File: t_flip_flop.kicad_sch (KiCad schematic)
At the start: 3 parts, among them U4 4011

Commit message: routing done
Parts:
- renumbered C2 to C13, R11 to R6, U4 to U5
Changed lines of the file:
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@@
   (symbol (lib_id "4xxx:4011") (at 92.71 39.37 0) (unit 1)
     (in_bom yes) (on_board yes) (fields_autoplaced)
-    (property "Reference" "U4" (id 0) (at 92.71 31.8602 0))
+    (property "Reference" "U5" (id 0) (at 92.71 31.8602 0))
     (property "Value" "4011" (id 1) (at 92.71 34.3971 0))
     (property "Footprint" "Package_SO:SOIC-14_3.9x8.7mm_P1.27mm" (id 2) (at 92.71 39.37 0)
@@
   (symbol (lib_id "power:VDD") (at 29.21 36.83 0) (unit 1)
     (in_bom yes) (on_board yes)
-    (property "Reference" "#PWR011" (id 0) (at 29.21 40.64 0)
+    (property "Reference" "#PWR024" (id 0) (at 29.21 40.64 0)
       (effects (font (size 1.27 1.27)) hide)
     )
@@
   (symbol (lib_id "4xxx:4011") (at 92.71 59.69 0) (unit 2)
     (in_bom yes) (on_board yes) (fields_autoplaced)
-    (property "Reference" "U4" (id 0) (at 92.71 52.1802 0))
+    (property "Reference" "U5" (id 0) (at 92.71 52.1802 0))
     (property "Value" "4011" (id 1) (at 92.71 54.7171 0))
     (property "Footprint" "Package_SO:SOIC-14_3.9x8.7mm_P1.27mm" (id 2) (at 92.71 59.69 0)
@@
   (symbol (lib_id "4xxx:4011") (at 115.57 41.91 0) (unit 3)
     (in_bom yes) (on_board yes) (fields_autoplaced)
-    (property "Reference" "U4" (id 0) (at 115.57 34.4002 0))
+    (property "Reference" "U5" (id 0) (at 115.57 34.4002 0))
     (property "Value" "4011" (id 1) (at 115.57 36.9371 0))
     (property "Footprint" "Package_SO:SOIC-14_3.9x8.7mm_P1.27mm" (id 2) (at 115.57 41.91 0)
@@
   (symbol (lib_id "4xxx:4011") (at 115.57 57.15 0) (unit 4)
     (in_bom yes) (on_board yes) (fields_autoplaced)
-    (property "Reference" "U4" (id 0) (at 115.57 49.6402 0))
+    (property "Reference" "U5" (id 0) (at 115.57 49.6402 0))
     (property "Value" "4011" (id 1) (at 115.57 52.1771 0))
     (property "Footprint" "Package_SO:SOIC-14_3.9x8.7mm_P1.27mm" (id 2) (at 115.57 57.15 0)
@@
   (symbol (lib_id "Device:C") (at 57.785 53.34 0) (unit 1)
     (in_bom yes) (on_board yes) (fields_autoplaced)
-    (property "Reference" "C2" (id 0) (at 60.706 52.5053 0)
+    (property "Reference" "C13" (id 0) (at 60.706 52.5053 0)
       (effects (font (size 1.27 1.27)) (justify left))
     )
@@
   (symbol (lib_id "Device:R") (at 68.58 53.34 180) (unit 1)
     (in_bom yes) (on_board yes) (fields_autoplaced)
-    (property "Reference" "R11" (id 0) (at 70.358 52.5053 0)
+    (property "Reference" "R6" (id 0) (at 70.358 52.5053 0)
       (effects (font (size 1.27 1.27)) (justify right))
     )
@@
   (symbol (lib_id "power:VSS") (at 57.785 57.15 180) (unit 1)
     (in_bom yes) (on_board yes) (fields_autoplaced)
-    (property "Reference" "#PWR014" (id 0) (at 57.785 53.34 0)
+    (property "Reference" "#PWR026" (id 0) (at 57.785 53.34 0)
       (effects (font (size 1.27 1.27)) hide)
     )
@@
   (symbol (lib_id "power:VSS") (at 29.21 62.23 180) (unit 1)
     (in_bom yes) (on_board yes) (fields_autoplaced)
-    (property "Reference" "#PWR012" (id 0) (at 29.21 58.42 0)
+    (property "Reference" "#PWR025" (id 0) (at 29.21 58.42 0)
       (effects (font (size 1.27 1.27)) hide)
     )
@@
   (symbol (lib_id "4xxx:4011") (at 29.21 49.53 0) (unit 5)
     (in_bom yes) (on_board yes) (fields_autoplaced)
-    (property "Reference" "U4" (id 0) (at 35.052 48.6953 0)
+    (property "Reference" "U5" (id 0) (at 35.052 48.6953 0)
       (effects (font (size 1.27 1.27)) (justify left))
     )

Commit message: ready to order
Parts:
- U5: value 4011 -> 4093; symbol 4xxx:4011 -> 4xxx:HEF4093B; JLC C194334 -> C194332
- renumbered C13 to C17
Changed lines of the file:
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@@
     (effects (font (size 1.27 1.27)) (justify left))
   )
-  (symbol (lib_id "4xxx:4011") (at 92.71 39.37 0) (unit 1)
+  (symbol (lib_id "4xxx:HEF4093B") (at 92.71 39.37 0) (unit 1)
     (in_bom yes) (on_board yes) (fields_autoplaced)
     (property "Reference" "U5" (id 0) (at 92.71 31.8602 0))
-    (property "Value" "4011" (id 1) (at 92.71 34.3971 0))
+    (property "Value" "4093" (id 1) (at 92.71 34.3971 0))
     (property "Footprint" "Package_SO:SOIC-14_3.9x8.7mm_P1.27mm" (id 2) (at 92.71 39.37 0)
       (effects (font (size 1.27 1.27)) hide)
     )
-    (property "Datasheet" "https://datasheet.lcsc.com/lcsc/1811031937_HGSEMI-CD4011BM-TR_C194334.pdf" (id 3) (at 92.71 39.37 0)
-      (effects (font (size 1.27 1.27)) hide)
-    )
-    (property "JLC" "C194334" (id 4) (at 92.71 39.37 0)
+    (property "Datasheet" "https://datasheet.lcsc.com/lcsc/2107091824_HGSEMI-CD4093BM-TR_C194332.pdf" (id 3) (at 92.71 39.37 0)
+      (effects (font (size 1.27 1.27)) hide)
+    )
+    (property "JLC" "C194332" (id 4) (at 92.71 39.37 0)
       (effects (font (size 1.27 1.27)) hide)
     )
@@
   (symbol (lib_id "power:VDD") (at 29.21 36.83 0) (unit 1)
     (in_bom yes) (on_board yes)
-    (property "Reference" "#PWR024" (id 0) (at 29.21 40.64 0)
+    (property "Reference" "#PWR026" (id 0) (at 29.21 40.64 0)
       (effects (font (size 1.27 1.27)) hide)
     )
@@
     (pin "1")
   )
-  (symbol (lib_id "4xxx:4011") (at 92.71 59.69 0) (unit 2)
+  (symbol (lib_id "4xxx:HEF4093B") (at 92.71 59.69 0) (unit 2)
     (in_bom yes) (on_board yes) (fields_autoplaced)
     (property "Reference" "U5" (id 0) (at 92.71 52.1802 0))
-    (property "Value" "4011" (id 1) (at 92.71 54.7171 0))
+    (property "Value" "4093" (id 1) (at 92.71 54.7171 0))
     (property "Footprint" "Package_SO:SOIC-14_3.9x8.7mm_P1.27mm" (id 2) (at 92.71 59.69 0)
       (effects (font (size 1.27 1.27)) hide)
     )
-    (property "Datasheet" "https://datasheet.lcsc.com/lcsc/1811031937_HGSEMI-CD4011BM-TR_C194334.pdf" (id 3) (at 92.71 59.69 0)
-      (effects (font (size 1.27 1.27)) hide)
-    )
-    (property "JLC" "C194334" (id 4) (at 92.71 59.69 0)
-      (effects (font (size 1.27 1.27)) hide)
-    )
-    (pin "1")
-    (pin "2")
-    (pin "3")
-    (pin "4")
-    (pin "5")
-    (pin "6")
-    (pin "10")
-    (pin "8")
-    (pin "9")
-    (pin "11")
-    (pin "12")
-    (pin "13")
-    (pin "14")
-    (pin "7")
-  )
-  (symbol (lib_id "4xxx:4011") (at 115.57 41.91 0) (unit 3)
+    (property "Datasheet" "https://datasheet.lcsc.com/lcsc/2107091824_HGSEMI-CD4093BM-TR_C194332.pdf" (id 3) (at 92.71 59.69 0)
+      (effects (font (size 1.27 1.27)) hide)
+    )
+    (property "JLC" "C194332" (id 4) (at 92.71 59.69 0)
+      (effects (font (size 1.27 1.27)) hide)
+    )
+    (pin "1")
+    (pin "2")
+    (pin "3")
+    (pin "4")
+    (pin "5")
+    (pin "6")
+    (pin "10")
+    (pin "8")
+    (pin "9")
+    (pin "11")
+    (pin "12")
+    (pin "13")
+    (pin "14")
+    (pin "7")
+  )
+  (symbol (lib_id "4xxx:HEF4093B") (at 115.57 41.91 0) (unit 3)
     (in_bom yes) (on_board yes) (fields_autoplaced)
     (property "Reference" "U5" (id 0) (at 115.57 34.4002 0))
-    (property "Value" "4011" (id 1) (at 115.57 36.9371 0))
+    (property "Value" "4093" (id 1) (at 115.57 36.9371 0))
     (property "Footprint" "Package_SO:SOIC-14_3.9x8.7mm_P1.27mm" (id 2) (at 115.57 41.91 0)
       (effects (font (size 1.27 1.27)) hide)
     )
-    (property "Datasheet" "https://datasheet.lcsc.com/lcsc/1811031937_HGSEMI-CD4011BM-TR_C194334.pdf" (id 3) (at 115.57 41.91 0)
-      (effects (font (size 1.27 1.27)) hide)
-    )
-    (property "JLC" "C194334" (id 4) (at 115.57 41.91 0)
-      (effects (font (size 1.27 1.27)) hide)
-    )
-    (pin "1")
-    (pin "2")
-    (pin "3")
-    (pin "4")
-    (pin "5")
-    (pin "6")
-    (pin "10")
-    (pin "8")
-    (pin "9")
-    (pin "11")
-    (pin "12")
-    (pin "13")
-    (pin "14")
-    (pin "7")
-  )
-  (symbol (lib_id "4xxx:4011") (at 115.57 57.15 0) (unit 4)
+    (property "Datasheet" "https://datasheet.lcsc.com/lcsc/2107091824_HGSEMI-CD4093BM-TR_C194332.pdf" (id 3) (at 115.57 41.91 0)
+      (effects (font (size 1.27 1.27)) hide)
+    )
+    (property "JLC" "C194332" (id 4) (at 115.57 41.91 0)
+      (effects (font (size 1.27 1.27)) hide)
+    )
+    (pin "1")
+    (pin "2")
+    (pin "3")
+    (pin "4")
+    (pin "5")
+    (pin "6")
+    (pin "10")
+    (pin "8")
+    (pin "9")
+    (pin "11")
+    (pin "12")
+    (pin "13")
+    (pin "14")
+    (pin "7")
+  )
+  (symbol (lib_id "4xxx:HEF4093B") (at 115.57 57.15 0) (unit 4)
     (in_bom yes) (on_board yes) (fields_autoplaced)
     (property "Reference" "U5" (id 0) (at 115.57 49.6402 0))
-    (property "Value" "4011" (id 1) (at 115.57 52.1771 0))
+    (property "Value" "4093" (id 1) (at 115.57 52.1771 0))
     (property "Footprint" "Package_SO:SOIC-14_3.9x8.7mm_P1.27mm" (id 2) (at 115.57 57.15 0)
       (effects (font (size 1.27 1.27)) hide)
     )
-    (property "Datasheet" "https://datasheet.lcsc.com/lcsc/1811031937_HGSEMI-CD4011BM-TR_C194334.pdf" (id 3) (at 115.57 57.15 0)
-      (effects (font (size 1.27 1.27)) hide)
-    )
-    (property "JLC" "C194334" (id 4) (at 115.57 57.15 0)
+    (property "Datasheet" "https://datasheet.lcsc.com/lcsc/2107091824_HGSEMI-CD4093BM-TR_C194332.pdf" (id 3) (at 115.57 57.15 0)
+      (effects (font (size 1.27 1.27)) hide)
+    )
+    (property "JLC" "C194332" (id 4) (at 115.57 57.15 0)
       (effects (font (size 1.27 1.27)) hide)
     )
@@
   (symbol (lib_id "Device:C") (at 57.785 53.34 0) (unit 1)
     (in_bom yes) (on_board yes) (fields_autoplaced)
-    (property "Reference" "C13" (id 0) (at 60.706 52.5053 0)
+    (property "Reference" "C17" (id 0) (at 60.706 52.5053 0)
       (effects (font (size 1.27 1.27)) (justify left))
     )
@@
   (symbol (lib_id "power:VSS") (at 57.785 57.15 180) (unit 1)
     (in_bom yes) (on_board yes) (fields_autoplaced)
-    (property "Reference" "#PWR026" (id 0) (at 57.785 53.34 0)
+    (property "Reference" "#PWR028" (id 0) (at 57.785 53.34 0)
       (effects (font (size 1.27 1.27)) hide)
     )
@@
   (symbol (lib_id "power:VSS") (at 29.21 62.23 180) (unit 1)
     (in_bom yes) (on_board yes) (fields_autoplaced)
-    (property "Reference" "#PWR025" (id 0) (at 29.21 58.42 0)
+    (property "Reference" "#PWR027" (id 0) (at 29.21 58.42 0)
       (effects (font (size 1.27 1.27)) hide)
     )
@@
     (pin "1")
   )
-  (symbol (lib_id "4xxx:4011") (at 29.21 49.53 0) (unit 5)
+  (symbol (lib_id "4xxx:HEF4093B") (at 29.21 49.53 0) (unit 5)
     (in_bom yes) (on_board yes) (fields_autoplaced)
     (property "Reference" "U5" (id 0) (at 35.052 48.6953 0)
       (effects (font (size 1.27 1.27)) (justify left))
     )
-    (property "Value" "4011" (id 1) (at 35.052 51.2322 0)
+    (property "Value" "4093" (id 1) (at 35.052 51.2322 0)
       (effects (font (size 1.27 1.27)) (justify left))
     )
@@
       (effects (font (size 1.27 1.27)) hide)
     )
-    (property "Datasheet" "https://datasheet.lcsc.com/lcsc/1811031937_HGSEMI-CD4011BM-TR_C194334.pdf" (id 3) (at 29.21 49.53 0)
-      (effects (font (size 1.27 1.27)) hide)
-    )
-    (property "JLC" "C194334" (id 4) (at 29.21 49.53 0)
-      (effects (font (size 1.27 1.27)) hide)
-    )
+    (property "Datasheet" "https://datasheet.lcsc.com/lcsc/2107091824_HGSEMI-CD4093BM-TR_C194332.pdf" (id 3) (at 29.21 49.53 0)
+      (effects (font (size 1.27 1.27)) hide)
+    )
+    (property "JLC" "C194332" (id 4) (at 29.21 49.53 0)
+      (effects (font (size 1.27 1.27)) hide)
+    )

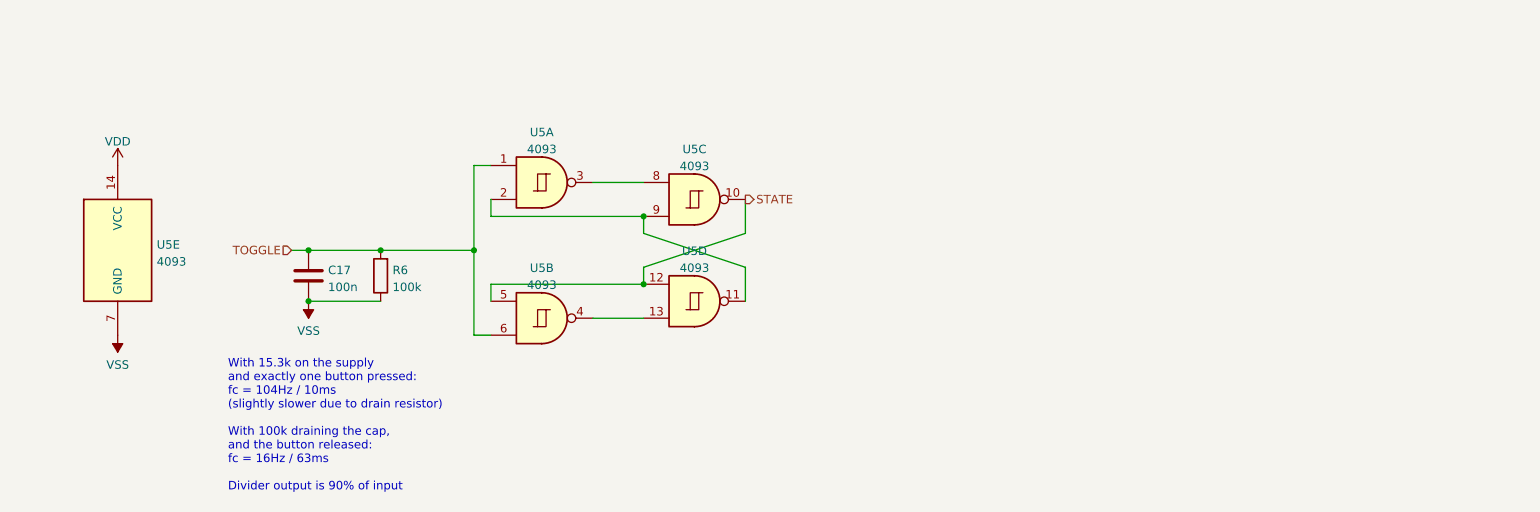
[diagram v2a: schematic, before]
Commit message: started fixing issues from V1
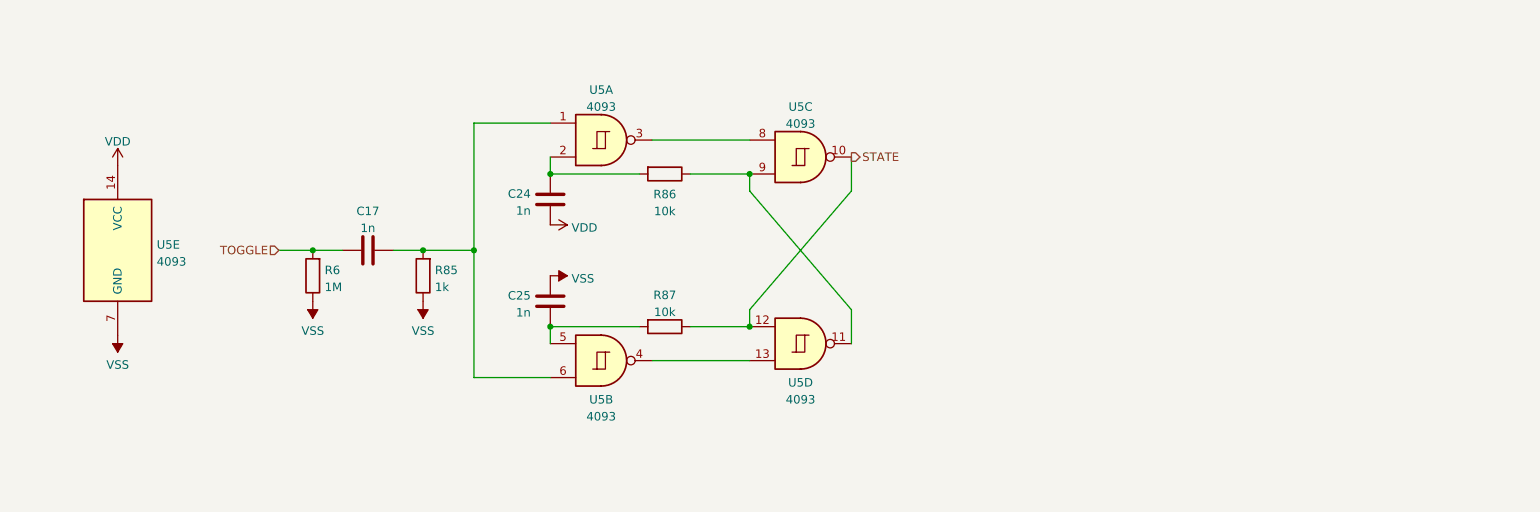
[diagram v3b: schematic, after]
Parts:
- added C24, C25: 1n, Capacitor_SMD:C_0402_1005Metric, symbol Device:C
- added R85: 1k, Resistor_SMD:R_0402_1005Metric, symbol Device:R
- added R86, R87: 10k, Resistor_SMD:R_0402_1005Metric, symbol Device:R
- C17: value 100n -> 1n; JLC C1525 -> C1523
- R6: value 100k -> 1M; JLC C25741 -> C26083
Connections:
- net STATE: now also R87.1; no longer U5.5
- net TOGGLE: no longer U5.1, U5.6
- net VDD: now also C24.1
- net VSS: now also C25.2, R85.1; no longer C17.2
- net at U5.11, U5.9: now also R86.1; no longer U5.2
- new net: C17.2, R85.2, U5.1, U5.6
- new net: C24.2, R86.2, U5.2
- new net: C25.1, R87.2, U5.5
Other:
- note removed: "With 15.3k on the supply and exactly one button pressed: fc = 104Hz / 10ms (slightly slower due to drain resistor) With 100k draining the cap, and the button released: fc = 16Hz / 63ms Divider output is 90% of input"
- moved on the sheet: C17, R6, U5A, U5B, U5C, U5D

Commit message: pre-re-layout
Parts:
- added C201: 100n, Capacitor_SMD:C_0402_1005Metric, symbol Device:C
- renumbered C17 to C202, C24 to C203, C25 to C204, R6 to R201, R85 to R202, R86 to R203, R87 to R204, U5 to U201
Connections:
- net VDD: now also C201.1
- net VSS: now also C201.2
- net PULSE: now reaches C202.2, R202.2, U201.1, U201.6
- net ~{Q}': now reaches C203.2, R203.2, U201.2
- net SET: now reaches U201.3, U201.8
- net Q': now reaches C204.1, R204.2, U201.5
- net RESET: now reaches U201.13, U201.4
- net ~{Q}: now reaches R203.1, U201.11, U201.9
- net STATE renamed Q
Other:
- note added: "CB"
- note added: "CC"
- note added: "RA"
- note added: "RB"
- note added: "RC"
- note added: "Rising-edge triggered toggle flip-flop"
- note added: "Values we have chosen: RIN*CB < 1e-9 (resolution/height) [i.e. unwanted RIN is < 1] RA*CB = 1e-3 (debounce) RB*CB = 1e-6 (pulse width) RC*CC = 1e-5 (feedback delay)"
- note added: "We assume the input is a switch. When depressed, it is Hi-Z. When pressed, it is Lo-Z to VDD. Summary: RIN*CB : min input-pulse duration required to trigger a toggle-pulse. also sets pulse height, so check this carefully! RA*CB : input-pulse resolution (ie. debounce). RB*CB : toggle-pulse duration. RC*CC : feedback delay. Feedback delay should be longer than toggle-pulse duration. ie. RC*CC > RB*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"
- moved on the sheet: U201C, U201D
